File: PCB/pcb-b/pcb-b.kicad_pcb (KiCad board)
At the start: 2 copper layers, 94.7 x 42 mm, 82 parts, among them J1 Conn_02x05_Counter_Clockwise, J2 Conn_02x05_Counter_Clockwise, K1 HK19F-DCxxV-SHC, Q1 BC817, Q10 BC817, Q11 TPCA8120,L1Q, Q13 TPCA8120,L1Q, Q14 BC817, Q15 BC817, Q19 BC817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

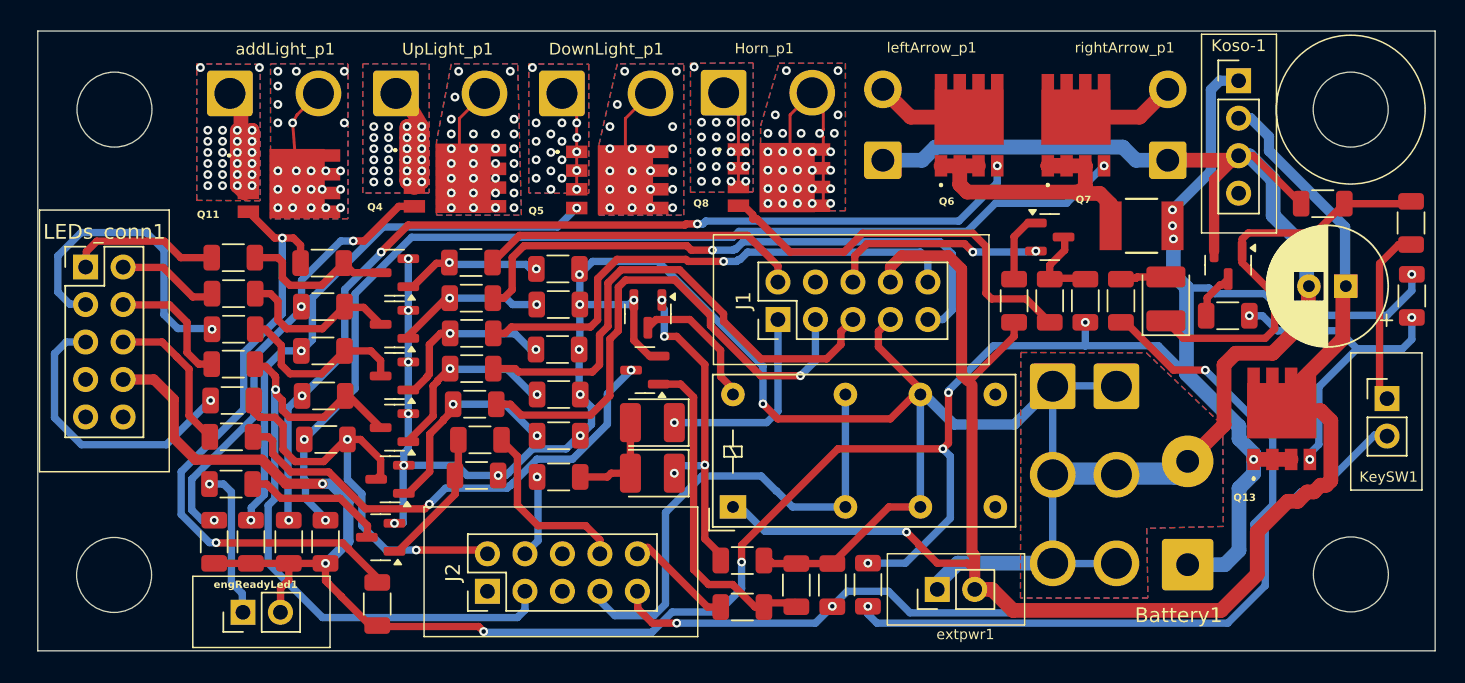
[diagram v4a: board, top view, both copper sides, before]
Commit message: Many changes and fixes
Electric schema A & B
	- Wrong (undefined) signals direction fixed
	- More readable schema getting: c_<signal> color has changed
	- Some pull-up resistors has been added for safing purpose
	- Wire connectors holes size reducing
	- Because Led indicatord uses less then 500mA, their wire connectors have been substituted by pin-header ones

PCB
	- Updates for schema changes
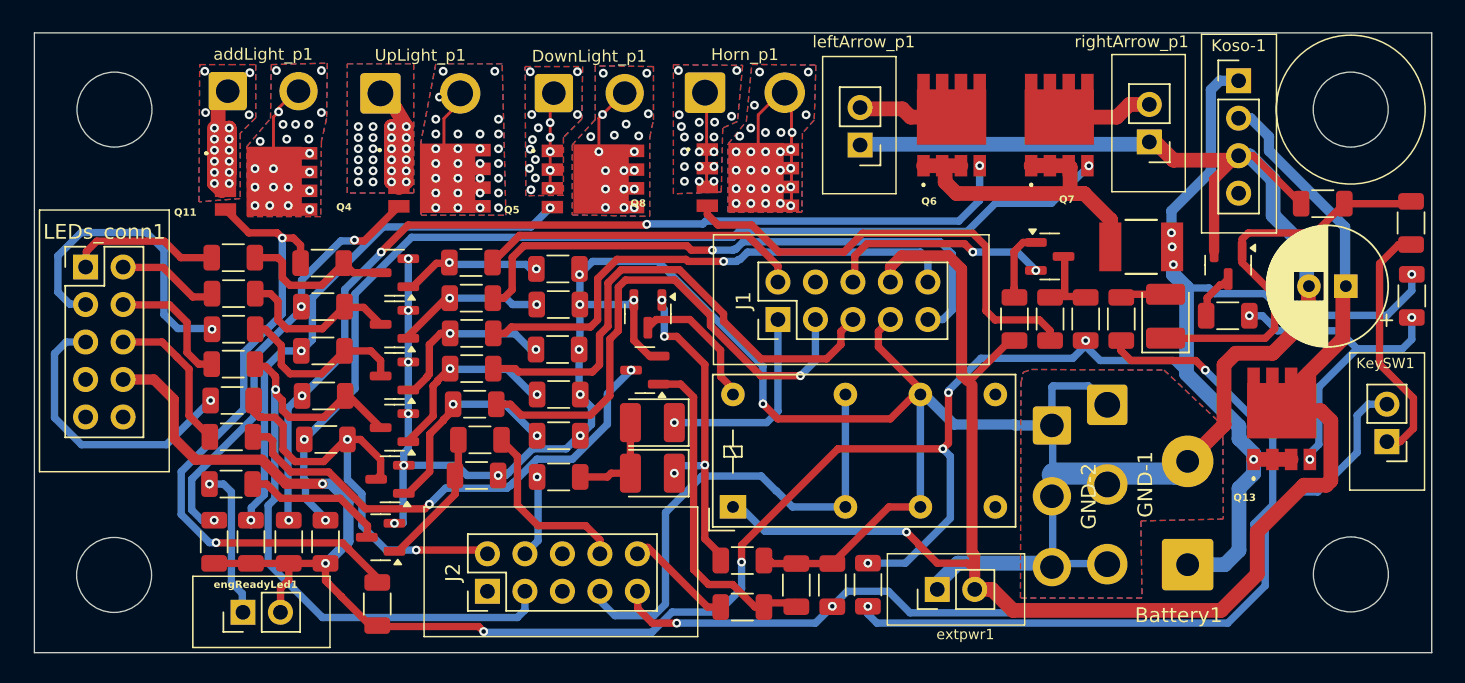
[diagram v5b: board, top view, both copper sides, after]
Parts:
- DownLight_p1, addLight_p1: footprint Connector_Wire:SolderWire-1.5sqmm_1x02_P6mm_D1.7mm_OD3mm -> Connector_Wire:SolderWire-0.75sqmm_1x02_P4.8mm_D1.25mm_OD2.3mm
- GND-1: footprint Connector_Wire:SolderWire-1.5sqmm_1x03_P6mm_D1.7mm_OD3mm -> Connector_Wire:SolderWire-1sqmm_1x03_P5.4mm_D1.4mm_OD2.7mm
- GND-2: footprint Connector_Wire:SolderWire-1.5sqmm_1x03_P6mm_D1.7mm_OD3mm -> Connector_Wire:SolderWire-0.75sqmm_1x03_P4.8mm_D1.25mm_OD2.3mm
- Horn_p1, UpLight_p1: footprint Connector_Wire:SolderWire-1.5sqmm_1x02_P6mm_D1.7mm_OD3mm -> Connector_Wire:SolderWire-1sqmm_1x02_P5.4mm_D1.4mm_OD2.7mm
- leftArrow_p1, rightArrow_p1: footprint Connector_Wire:SolderWire-0.75sqmm_1x02_P4.8mm_D1.25mm_OD2.3mm -> Connector_PinHeader_2.54mm:PinHeader_1x02_P2.54mm_Vertical
- moved KeySW1 2.92 mm to (193.8, 97.7), turned to 180 degrees
- moved GND-2 2.66 mm to (171.1, 96.6)
- moved Q8 2.11 mm to (150.5, 79.8)
- moved leftArrow_p1 1.86 mm to (158.1, 77.6), turned to 180 degrees
- moved rightArrow_p1 1.76 mm to (177.7, 77.4), turned to 180 degrees
- moved Q5 1.65 mm to (140.0, 79.9)
- moved Q11 1.56 mm to (117.8, 80.1)
- moved F2 1.43 mm to (177.2, 84.5)
- moved GND-1 1.40 mm to (174.8, 95.2)
- moved Q10 1.32 mm to (170.9, 85.2)
- moved Horn_p1 1.26 mm to (147.6, 74.0)
- moved R5 1.23 mm to (175.8, 89.4)
- moved RA23 1.23 mm to (168.6, 89.4)
- moved RA42 1.23 mm to (173.4, 89.4)
- moved RA7 1.23 mm to (171.0, 89.4)
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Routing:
- net Net-(KeySW1-Pin_1): track 12.0 -> 17.6 mm
- net Net-(Q8-G): track 27.4 -> 31.4 mm
- net Net-(Q6-S_1): track 21.9 -> 24.5 mm
- net Net-(KeySW1-Pin_2): track 43.6 -> 45.9 mm
- net Net-(Q5-G): track 38.3 -> 36.5 mm
- net Net-(Q11-G): track 42.6 -> 44.3 mm
- net +12V: track 184.8 -> 183.6 mm
- net Net-(Q7-G): track 72.0 -> 70.9 mm
- net Net-(Q4-G): track 30.2 -> 29.1 mm
- net tempPower: track 117.1 -> 116.0 mm
- net Net-(Q11-S_1): track 17.7 -> 16.7 mm, vias 26 -> 16
- net Net-(Q6-G): track 65.7 -> 65.0 mm
- net Net-(Q10-C): track 5.77 -> 5.22 mm
- net Net-(Q7-D_1): track 7.00 -> 6.46 mm
- net Net-(DownLight_p1-Pin_1): track 6.91 -> 6.60 mm, vias 18 -> 16
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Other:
- outline, holes or cut-outs redrawn

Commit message: Small enhancement
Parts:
- removed extpwr1: Conn_01x02, Connector_PinHeader_2.54mm:PinHeader_1x02_P2.54mm_Vertical
- added rearDevs1: Conn_01x02, Connector_PinHeader_2.54mm:PinHeader_1x02_P2.54mm_Vertical, F.Cu at (163.3, 107.7)
- R3, R7: moved to B.Cu
- moved R7 4.10 mm to (193.3, 82.8), turned to -90 degrees
- moved R4 1.07 mm to (195.4, 84.0)
- moved R2 0.93 mm to (195.4, 88.8)
- moved Q13 0.88 mm to (186.2, 95.5)
- moved R3 0.82 mm to (183.0, 88.3)
- moved C9 0.66 mm to (191.0, 86.5)
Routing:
- net o_keepAlive: track 70.2 -> 52.0 mm
- net GND: track 226.5 -> 237.6 mm, vias 14 -> 15
- net Net-(D1-K): track 27.2 -> 22.0 mm, vias 0 -> 1
- net Net-(Q6-S_1): track 24.5 -> 21.5 mm
- net Net-(KeySW1-Pin_2): track 45.9 -> 44.1 mm
- net Net-(Q13-G): track 22.5 -> 21.2 mm, vias 3 -> 2
- net Net-(KeySW1-Pin_1): track 17.6 -> 16.3 mm
- net tempPower: track 116.0 -> 114.9 mm
- net Net-(Q9-C): track 3.19 -> 2.62 mm, vias 0 -> 1
- net +12V: track 183.6 -> 183.7 mm, vias 13 -> 15
- added copper zone on B.Cu, net +12V
- added copper zone on F.Cu, net +12V
- added copper zone on F.Cu, net Net-(Q6-S_1)

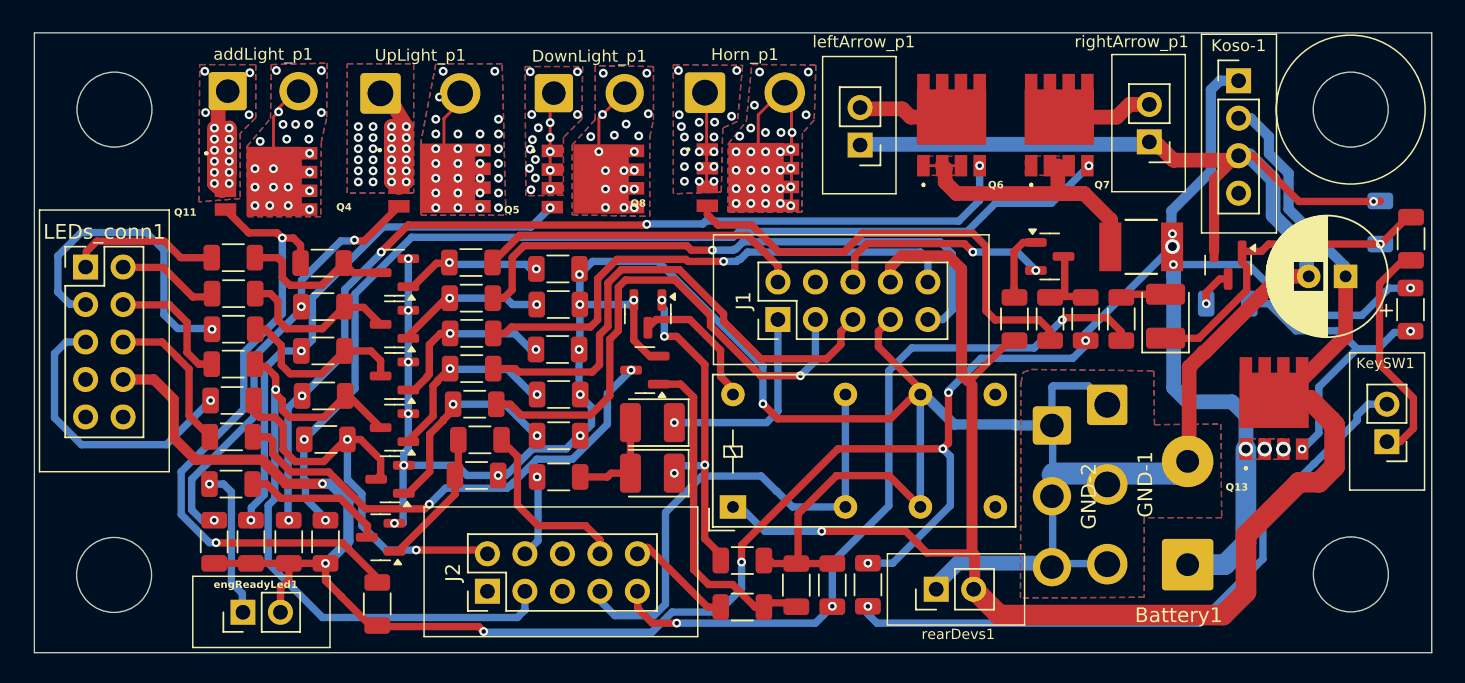
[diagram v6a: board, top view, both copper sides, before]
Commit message: Enhancements and size reduction
- Because the day-light needs just low current (<=500 mA), it no more uses the passive fuse. It has been replaced by a
  MSMF050-2 electronic fuse. Less passive fuses means less electric wires, then less chaos!
- A better components space distribution has reduced the PCB size (40.00mm x 90.11mm)
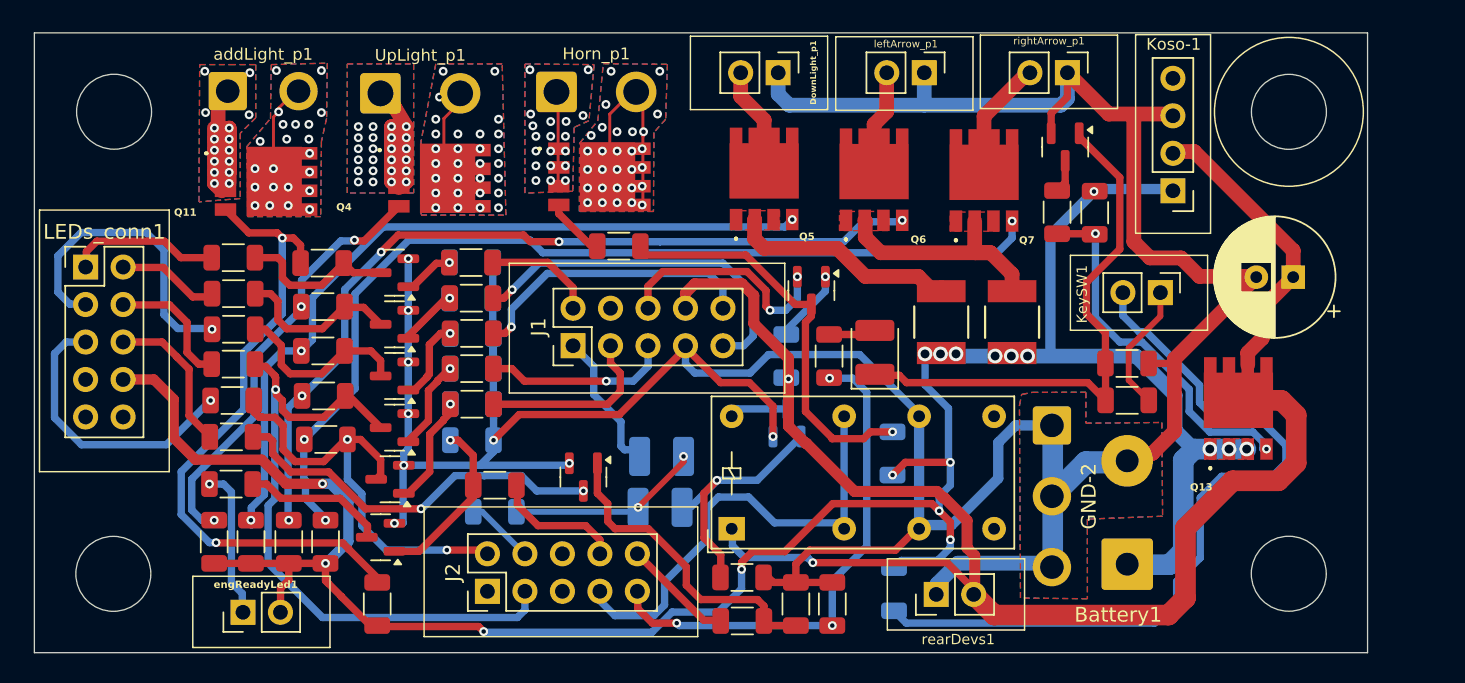
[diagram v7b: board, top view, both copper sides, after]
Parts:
- removed GND-1: ~, Connector_Wire:SolderWire-1sqmm_1x03_P5.4mm_D1.4mm_OD2.7mm
- added F1: MF-MSMF050-2, MF-MSMF050-2:FUSE_F050-2, F.Cu at (163.6, 89.6)
- D2, D3, Q3, R1, RA15, RA23, RA34, RA35, RA36, RA37, RA38, RA40, RA42: moved to B.Cu
- DownLight_p1: footprint Connector_Wire:SolderWire-0.75sqmm_1x02_P4.8mm_D1.25mm_OD2.3mm -> Connector_PinHeader_2.54mm:PinHeader_1x02_P2.54mm_Vertical
- F2: footprint MSMF050-2:FUSE_F050-2 -> MF-MSMF050-2:FUSE_F050-2
- R3, R7: moved to F.Cu
- RA13, RA14: value 120 -> 33K
- moved RA7 29.6 mm to (141.8, 84.5), turned to 0 degrees
- moved R2 22.4 mm to (174.0, 82.2)
- moved R4 22.1 mm to (176.2, 94.9), turned to 180 degrees
- moved R5 20.0 mm to (156.0, 91.9)
- moved D1 19.9 mm to (159.1, 91.7)
- moved R7 19.6 mm to (176.2, 92.4), turned to 180 degrees
- moved KeySW1 18.4 mm to (178.4, 87.6), turned to -90 degrees
- moved Q10 16.3 mm to (154.8, 87.5), turned to -90 degrees
- moved RA42 15.9 mm to (160.3, 98.5)
- moved RA23 15.7 mm to (153.1, 91.9)
- moved DownLight_p1 15.3 mm to (152.6, 72.7), turned to -90 degrees
- moved J1 14.0 mm to (138.7, 91.2)
- moved Q9 13.6 mm to (172.0, 77.7)
- moved R3 13.1 mm to (171.4, 82.2), turned to -90 degrees
- moved Q3 12.0 mm to (153.2, 96.4), turned to 90 degrees
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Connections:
- DownLight_p1 pad 1: Net-(DownLight_p1-Pin_1) -> GND
- Q5 pad 1: Net-(DownLight_p1-Pin_1) -> Net-(Q5-S_1)
- Q5 pad 2: Net-(DownLight_p1-Pin_1) -> Net-(Q5-S_1)
- Q5 pad 3: Net-(DownLight_p1-Pin_1) -> Net-(Q5-S_1)
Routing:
- net Net-(Q8-G): track 31.4 -> 4.27 mm
- net o_rightArrow: track 36.0 -> 12.3 mm, vias 1 -> 0
- net Net-(Q10-C): track 5.22 -> 27.6 mm, vias 0 -> 1
- net o_leftArrow: track 34.7 -> 12.7 mm, vias 0 -> 1
- net +12V: track 183.7 -> 165.3 mm, vias 15 -> 18
- net o_keepAlive: track 52.0 -> 35.5 mm
- net Net-(Q5-G): track 36.5 -> 52.6 mm
- net Net-(Q5-S_1): track 0.00 -> 15.7 mm
- net o_upLight: track 40.3 -> 24.7 mm
- net o_downLight: track 35.2 -> 19.8 mm
- net Net-(D1-K): track 22.0 -> 37.1 mm, vias 1 -> 0
- net o_addLight: track 22.1 -> 7.57 mm
- net Net-(KeySW1-Pin_2): track 44.1 -> 52.7 mm, vias 1 -> 0
- net GND: track 237.6 -> 229.8 mm, vias 15 -> 9
- net Net-(Q6-G): track 65.0 -> 57.5 mm
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- added copper zone on F.Cu, net Net-(Q5-S_1)
- removed copper zone on B.Cu, net Net-(DownLight_p1-Pin_1)
- removed copper zone on F.Cu, net Net-(DownLight_p1-Pin_1)
- removed copper zone on B.Cu, net Net-(DownLight_p1-Pin_2)
- removed copper zone on F.Cu, net Net-(DownLight_p1-Pin_2)
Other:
- board size 94.7 x 42 mm -> 90.3 x 42 mm

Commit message: Better arrangement of components and size reducing
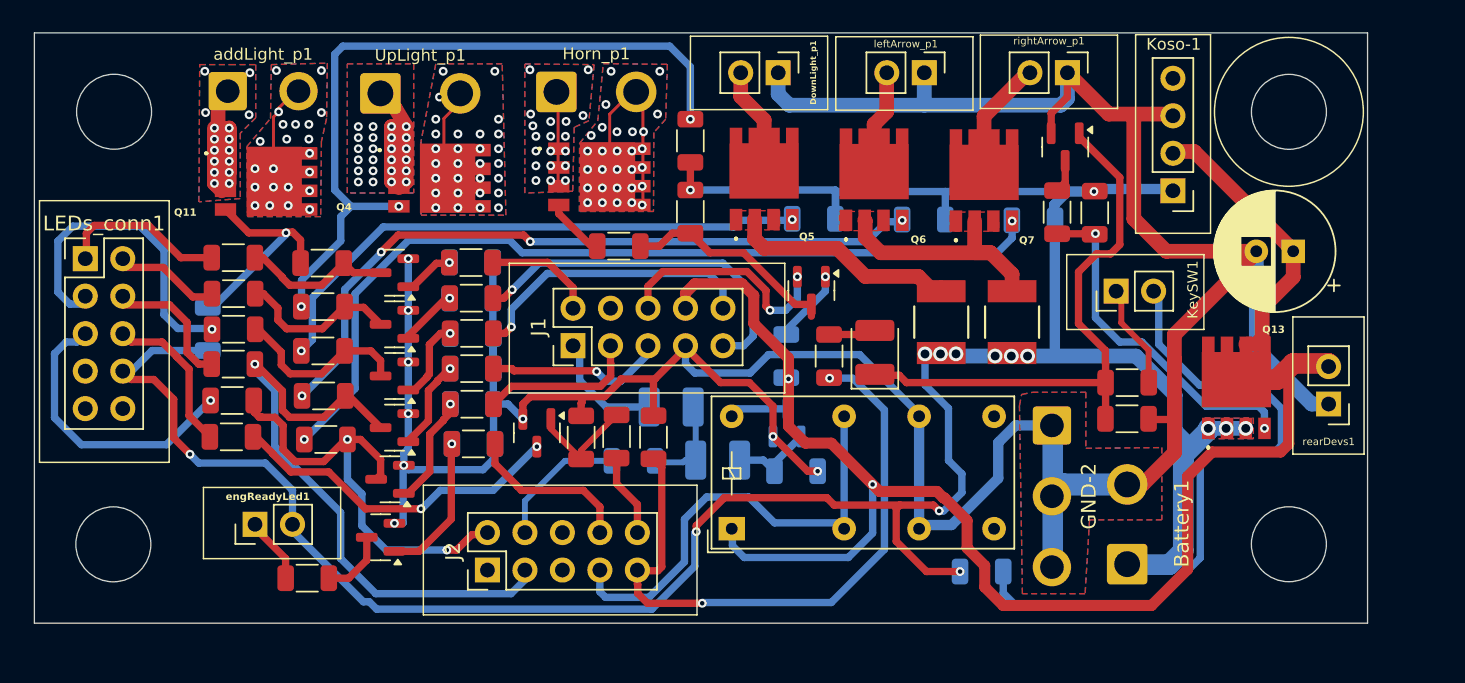
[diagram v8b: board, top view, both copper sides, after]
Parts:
- Battery1: footprint Connector_Wire:SolderWire-0.75sqmm_1x02_P7mm_D1.25mm_OD3.5mm -> Connector_Wire:SolderWire-1sqmm_1x02_P5.4mm_D1.4mm_OD2.7mm
- RA24, RA26, RA27, RA28, RA8: moved to B.Cu
- RA42: moved to F.Cu
- moved RA28 52.7 mm to (169.8, 82.7), turned to 180 degrees
- moved RA27 48.2 mm to (162.4, 82.7), turned to 180 degrees
- moved RA26 44.0 mm to (155.0, 82.6), turned to 180 degrees
- moved RA25 42.2 mm to (146.6, 77.3)
- moved rearDevs1 29.6 mm to (189.8, 95.2), turned to 180 degrees
- moved RA24 21.9 mm to (113.9, 90.1)
- moved RA42 21.4 mm to (146.6, 82.1), turned to 90 degrees
- moved RA39 18.4 mm to (139.2, 97.4)
- moved R6 16.6 mm to (144.1, 97.4)
- moved RA17 15.1 mm to (141.6, 97.3), turned to -90 degrees
- moved RA15 10.0 mm to (142.8, 99.0)
- moved RA9 8.20 mm to (120.6, 107.0)
- moved RA8 8.08 mm to (153.8, 99.7)
- moved R1 6.06 mm to (166.3, 106.5), turned to 180 degrees
- moved engReadyLed1 6.02 mm to (117.1, 103.3)
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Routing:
- net Net-(Q11-G): track 44.3 -> 15.0 mm, vias 2 -> 1
- net +12V: track 165.3 -> 188.6 mm, vias 18 -> 15
- net Net-(Q4-G): track 29.1 -> 50.8 mm
- net Net-(Q5-G): track 52.6 -> 38.6 mm, vias 3 -> 2
- net Net-(Q20-B): track 21.2 -> 8.17 mm
- net Net-(Q10-C): track 27.6 -> 14.7 mm, vias 1 -> 0
- net Net-(D2-K): track 17.5 -> 5.94 mm, vias 1 -> 0
- net Net-(Q6-G): track 57.5 -> 48.5 mm, vias 5 -> 4
- net o_keepAlive: track 35.5 -> 43.5 mm, vias 3 -> 2
- net Net-(KeySW1-Pin_2): track 52.7 -> 45.2 mm
- net GND: track 229.8 -> 222.6 mm
- net Net-(D2-A): track 13.1 -> 6.53 mm, vias 2 -> 0
- net Net-(Q7-G): track 65.6 -> 59.5 mm, vias 3 -> 2
- net Net-(engReadyLed1-Pin_1): track 10.2 -> 4.51 mm, vias 1 -> 0
- net Net-(Q21-C): track 9.76 -> 4.63 mm
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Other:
- board size 90.3 x 42 mm -> 90.3 x 40 mm
